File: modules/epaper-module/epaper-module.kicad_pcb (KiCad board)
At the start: 2 copper layers, 33 x 63.5 mm, 24 parts, among them J1 Conn_01x04, J2 Conn_01x04, Q1 Si1308EDL, U1 WSH-12561

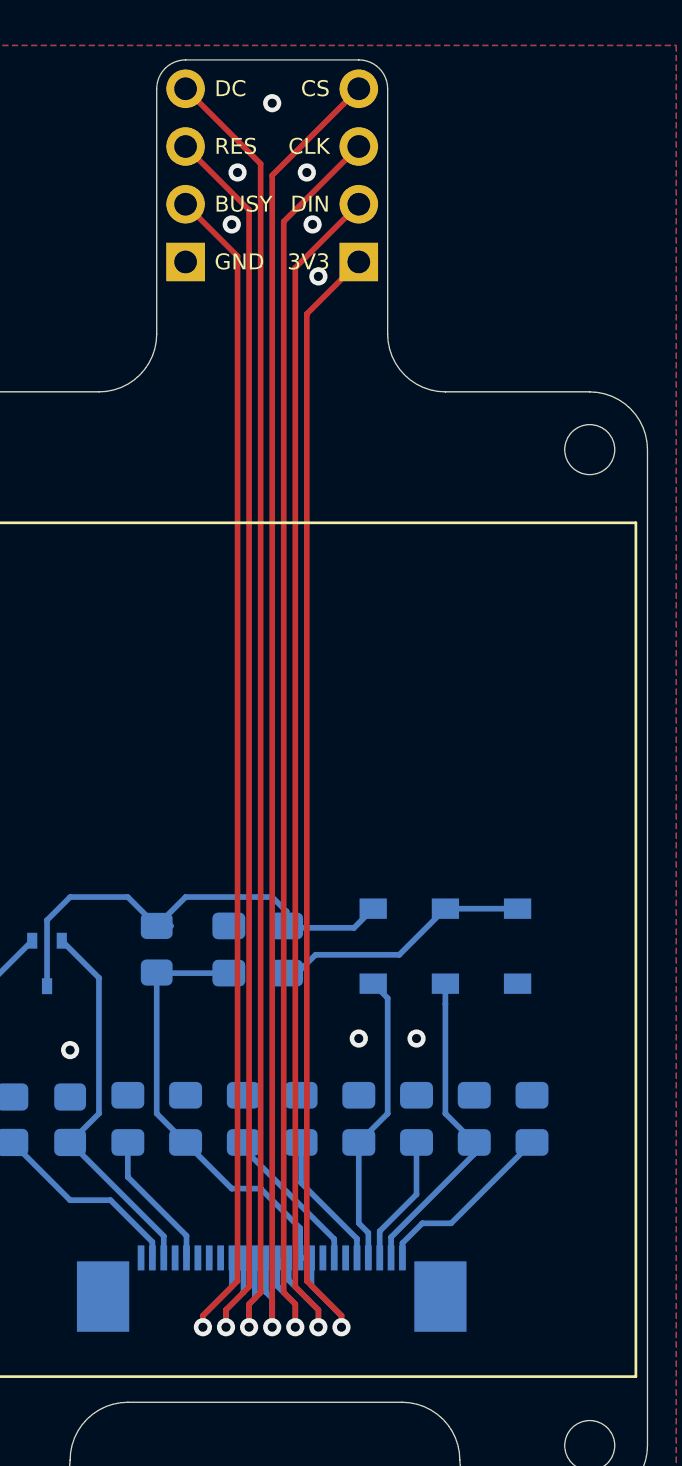
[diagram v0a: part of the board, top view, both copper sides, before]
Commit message: EPaper module: add voltage regulator and level switch
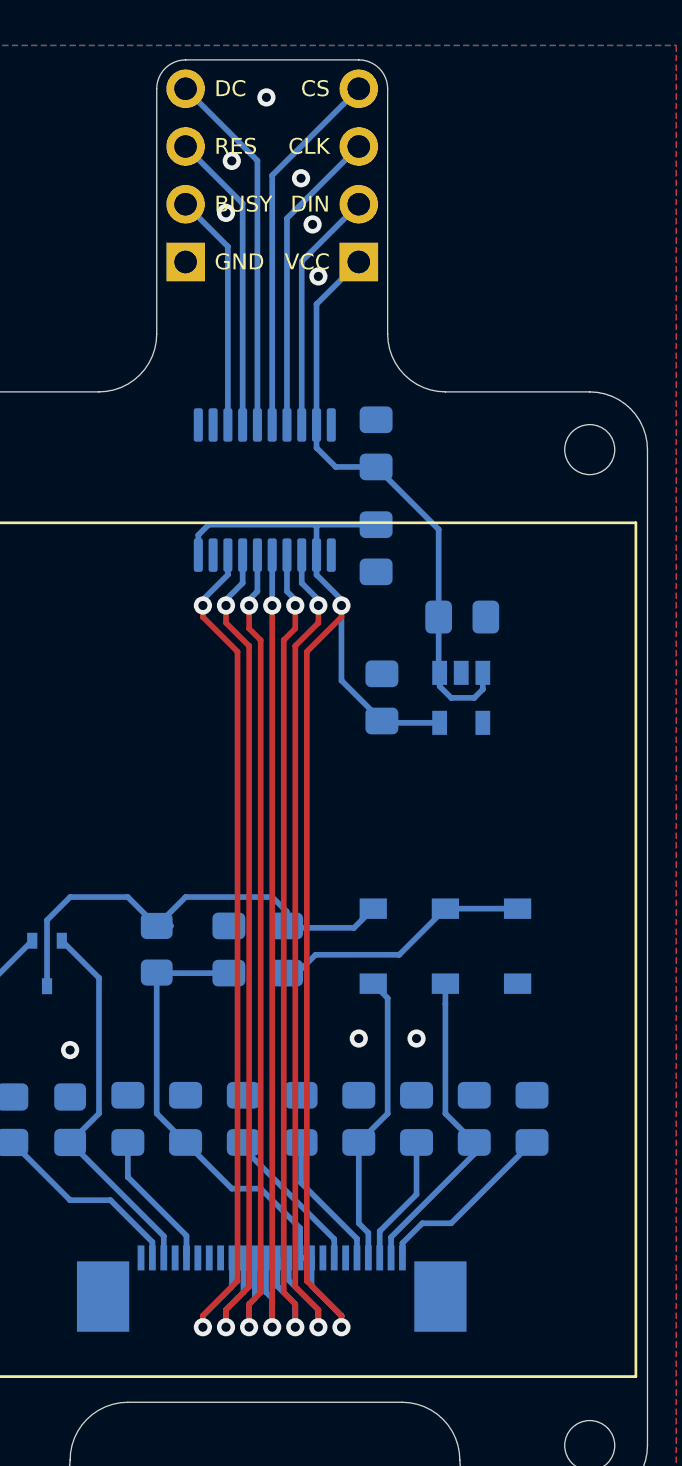
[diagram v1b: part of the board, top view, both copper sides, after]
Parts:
- added C1: 10uF, Capacitor_SMD:C_0805_2012Metric_Pad1.18x1.45mm_HandSolder, B.Cu at (87.9, 32.8)
- added C13: 100nF, Capacitor_SMD:C_0805_2012Metric_Pad1.18x1.45mm_HandSolder, B.Cu at (84.1, 29.7)
- added C14: 100nF, Capacitor_SMD:C_0805_2012Metric_Pad1.18x1.45mm_HandSolder, B.Cu at (84.1, 25.1)
- added C8: 4.7uF, Capacitor_SMD:C_0805_2012Metric_Pad1.18x1.45mm_HandSolder, B.Cu at (84.3, 36.3)
- added U2: MIC5504-3.3YM5, Package_TO_SOT_SMD:SOT-23-5, B.Cu at (87.8, 36.3)
- added U3: TXS0108EPW, Package_SO:TSSOP-20_4.4x6.5mm_P0.65mm, B.Cu at (79.2, 27.2)
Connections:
- J2 pad 1: +3V3 -> VCC
- U1 pad 10: /RES -> /RES'
- U1 pad 11: /DC -> /DC'
- U1 pad 12: /CS -> /CS'
- U1 pad 13: /CLK -> /CLK'
- U1 pad 14: /DIN -> /DIN'
- U1 pad 9: /BUSY -> /BUSY'
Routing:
- net /BUSY: track 55.1 -> 10.5 mm, vias 1 -> 0
- net /DIN: track 54.8 -> 10.8 mm, vias 1 -> 0
- net /CLK: track 56.9 -> 13.6 mm, vias 1 -> 0
- net /RES: track 56.4 -> 13.3 mm, vias 1 -> 0
- net /CS: track 59.2 -> 16.4 mm, vias 1 -> 0
- net /DC: track 58.7 -> 16.1 mm, vias 1 -> 0
- net /BUSY': track 0.00 -> 39.8 mm, vias 0 -> 2
- net /DIN': track 0.00 -> 39.0 mm, vias 0 -> 2
- net /RES': track 0.00 -> 38.0 mm, vias 0 -> 2
- net /CLK': track 0.00 -> 37.9 mm, vias 0 -> 2
- net /DC': track 0.00 -> 37.2 mm, vias 0 -> 2
- net /CS': track 0.00 -> 37.1 mm, vias 0 -> 2
- net VCC: track 0.00 -> 26.1 mm
- net +3V3: track 71.6 -> 77.5 mm, vias 1 -> 2
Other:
- board text added: "VCC"
- board text removed: "3V3"

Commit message: EPaper module: split display into display itself and connector
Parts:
- removed U1: WSH-12561, epaper-module:WSH-12561
- added DS1: WSH-12561, project_components:WSH-12561, F.Cu at (156.3, 96.5)
- added JP1: Jumper_NC_Dual, Jumper:SolderJumper-3_P2.0mm_Open_TrianglePad1.0x1.5mm, B.Cu at (145.7, 88.0)
- added XDS1: WSH-12561-FFC-MP, Connector_FFC-FPC:TE_2-1734839-4_1x24-1MP_P0.5mm_Horizontal, B.Cu at (156.3, 111.8)
- L1: value 10H -> 10uH; footprint Inductor_SMD:L_0805_2012Metric_Pad1.15x1.40mm_HandSolder -> Inductor_SMD:L_TDK_NLV25_2.5x2.0mm
- moved C1 91.4 mm to (164.7, 82.3)
- moved C10 91.4 mm to (162.7, 104.4)
- moved C11 91.4 mm to (165.2, 104.4)
- moved C3 91.4 mm to (157.0, 96.9)
- moved C7 91.4 mm to (155.1, 104.4)
- moved C8 91.4 mm to (161.2, 85.8)
- moved D1 91.4 mm to (164.0, 96.8)
- moved D2 91.4 mm to (167.1, 96.8)
- moved D3 91.4 mm to (160.8, 96.8)
- moved H1 91.4 mm to (142.4, 74.9)
- moved H2 91.4 mm to (170.3, 74.9)
- moved R1 91.4 mm to (144.9, 104.4)
- moved R2 91.4 mm to (147.4, 104.4)
- moved C12 91.4 mm to (167.8, 104.4)
- moved C13 91.4 mm to (160.9, 79.3)
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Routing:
- net /BS: track 0.00 -> 40.8 mm
- net +3V3: track 77.5 -> 89.9 mm
- net Net-(C3-Pad2): track 20.7 -> 19.5 mm
- net Net-(Q1-Pad1): track 19.3 -> 18.6 mm
- net GND: vias 9 -> 7
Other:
- board text added: "1.54inch E-Paper"
- board text added: "3-line"
- board text added: "4-line"
- board text added: "BS"

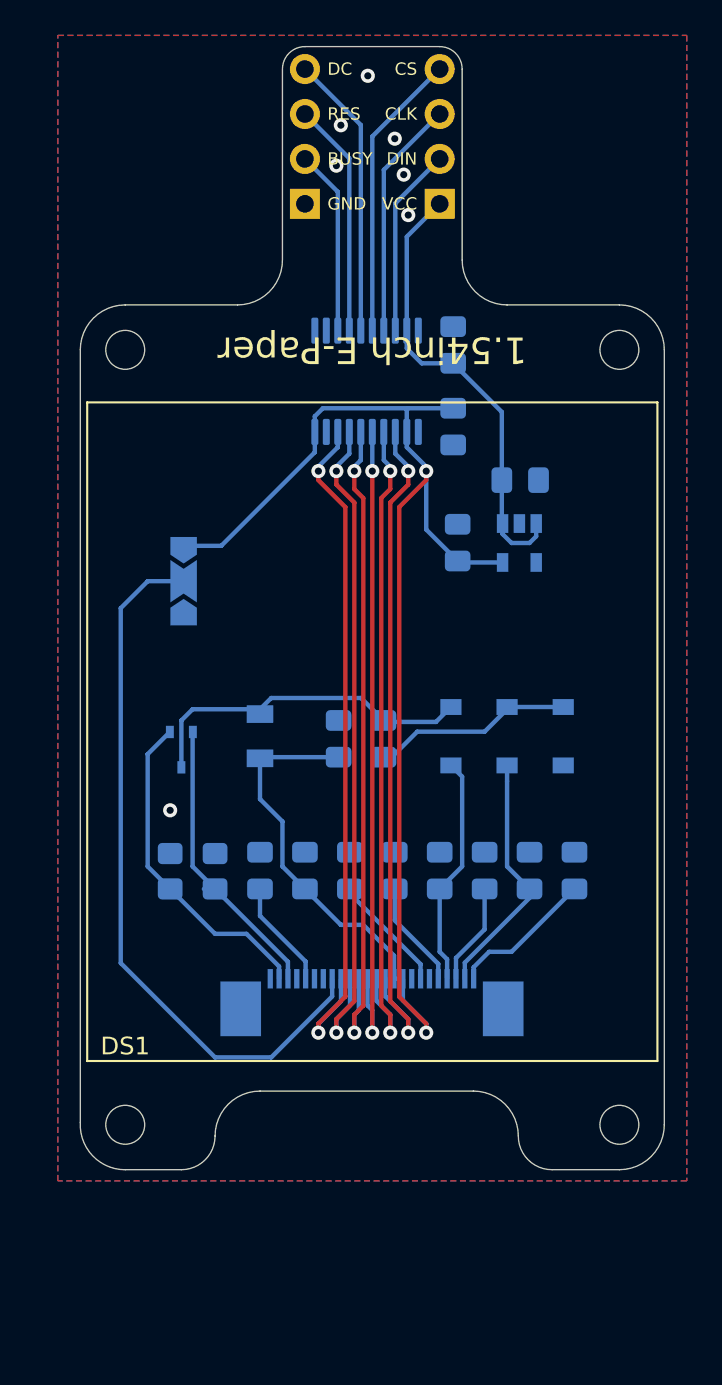
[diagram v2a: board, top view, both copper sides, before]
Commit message: EPaper module: rotate board
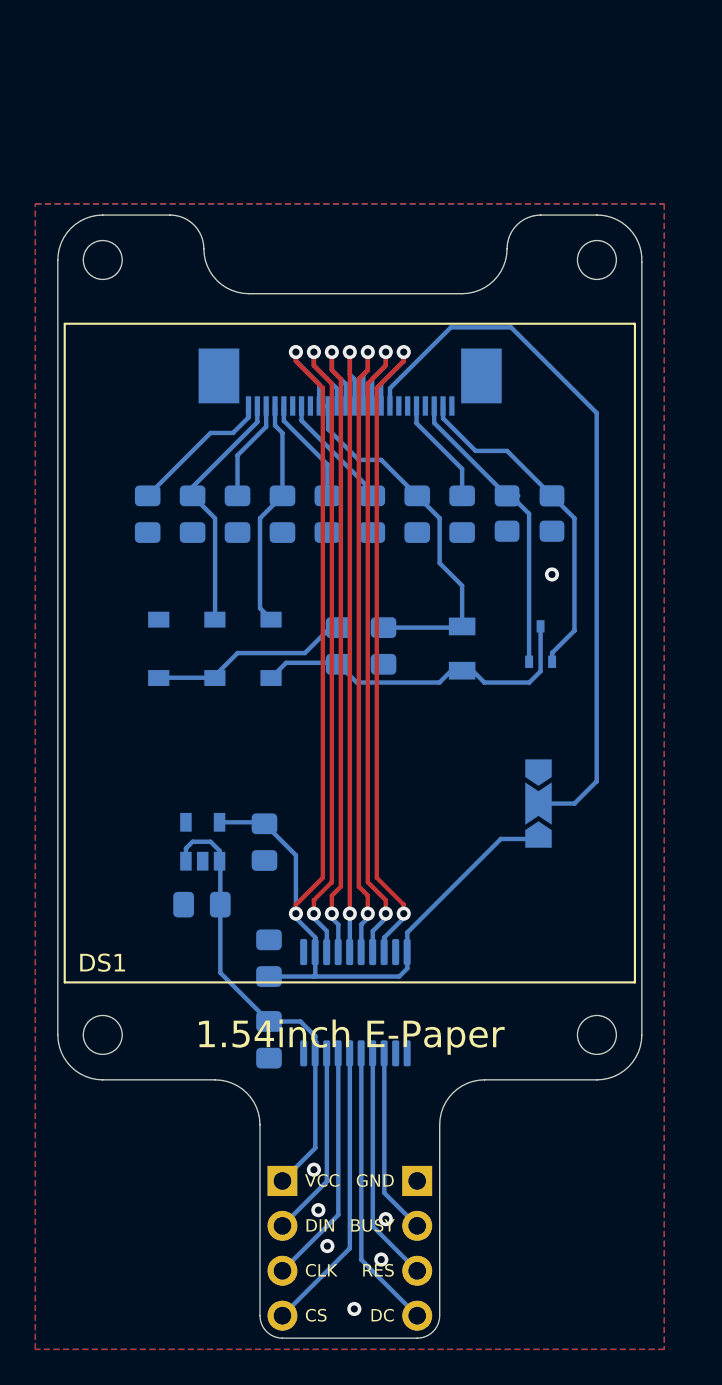
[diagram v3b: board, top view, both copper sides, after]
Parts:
- moved H4 57.0 mm to (141.1, 69.8), turned to 180 degrees
- moved J2 56.0 mm to (151.3, 121.9), turned to 180 degrees
- moved H3 55.7 mm to (169.0, 69.8), turned to 180 degrees
- moved J1 55.6 mm to (158.9, 121.9), turned to 180 degrees
- moved H2 48.5 mm to (141.1, 113.7), turned to 180 degrees
- moved H1 47.0 mm to (169.0, 113.7), turned to 180 degrees
- moved C14 40.6 mm to (150.5, 113.9), turned to 270 degrees
- moved U3 35.1 mm to (155.4, 111.8), turned to 270 degrees
- moved XDS1 35.1 mm to (155.1, 76.8), turned to 0 degrees
- moved C13 31.8 mm to (150.5, 109.3), turned to 90 degrees
- moved C12 31.4 mm to (143.6, 84.2), turned to 270 degrees
- moved C1 30.0 mm to (146.7, 106.3), turned to 180 degrees
- moved R1 29.6 mm to (166.5, 84.2), turned to 270 degrees
- moved C11 27.7 mm to (146.2, 84.2), turned to 270 degrees
- moved R2 26.1 mm to (164.0, 84.2), turned to 270 degrees
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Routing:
- net Net-(Q1-Pad2): track 16.9 -> 17.5 mm
- net Net-(Q1-Pad1): track 18.6 -> 19.1 mm
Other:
- outline, holes or cut-outs redrawn

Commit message: EPaper module: correct soldermask bridges
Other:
- rule pad_to_mask_clearance: 0.051 -> 0.05
- rule solder_mask_min_width: 0.25 -> 0.1
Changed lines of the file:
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@@
     (pad_size 0.3 0.3)
     (pad_drill 0)
-    (pad_to_mask_clearance 0.051)
-    (solder_mask_min_width 0.25)
+    (pad_to_mask_clearance 0.05)
+    (solder_mask_min_width 0.1)
     (aux_axis_origin 156.337 93.345)
     (grid_origin 155.057 108.98)
